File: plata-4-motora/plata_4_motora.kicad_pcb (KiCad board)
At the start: 2 copper layers, 141 x 90 mm, 28 parts, among them M0 мотор 0, M1 мотор 1, M2 мотор 2, M3 мотор 3, U0B S2209, U0T S2209, U1B S2209, U1T S2209, U2B S2209, U2T S2209, U3B S2209, U3T S2209

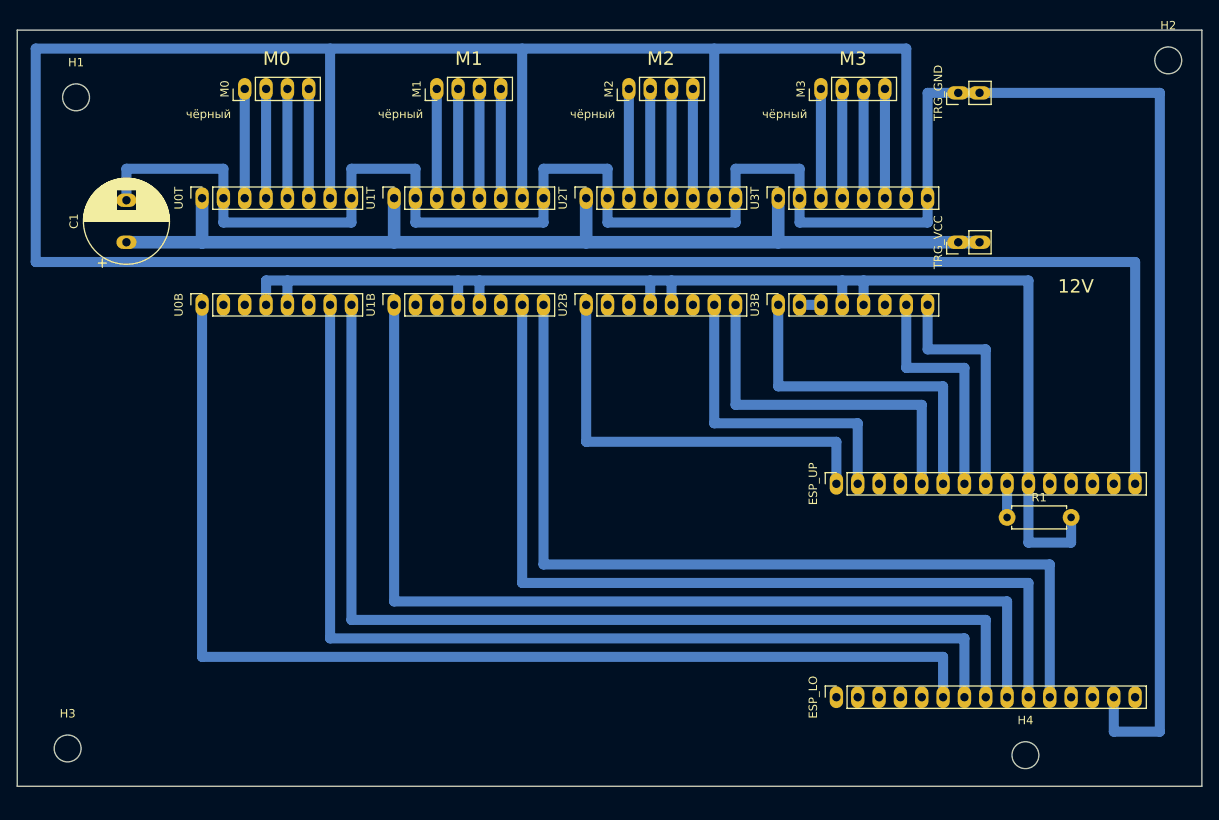
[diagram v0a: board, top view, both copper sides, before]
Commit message: Плата 4 моторов: компактная 92x92 (рисунок 65x89) под заготовку 100x100 — драйверы 2+2, ESP посередине; G-code за одну установку; вики 9.7–9.9
Co-Authored-By: Claude Fable 5.1 <noreply@anthropic.com>
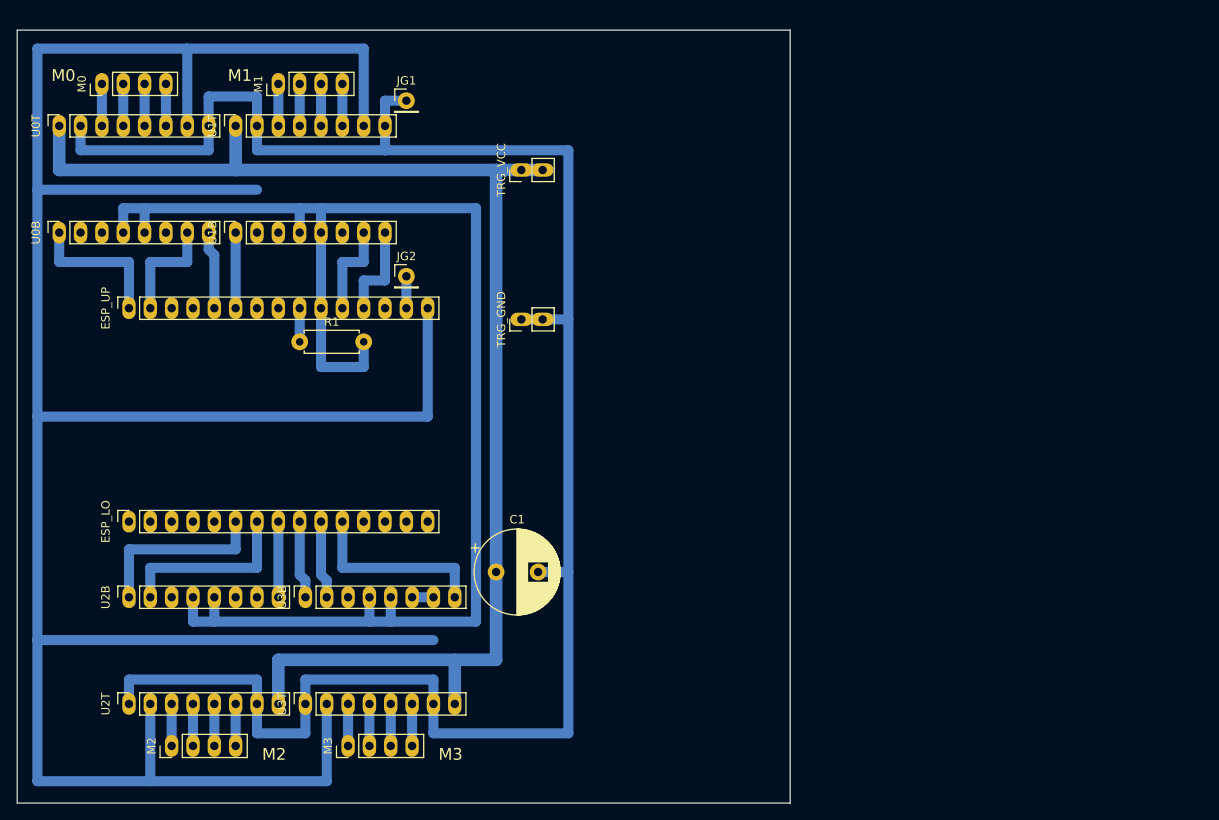
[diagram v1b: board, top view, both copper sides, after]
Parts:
- removed H1, H2, H3, H4: MountingHole_3.2mm_M3, MountingHole_3.2mm_M3
- added JG1: PinHeader_1x01_P2.54mm_Vertical, PinHeader_1x01_P2.54mm_Vertical, F.Cu at (46.3, 8.40)
- added JG2: PinHeader_1x01_P2.54mm_Vertical, PinHeader_1x01_P2.54mm_Vertical, F.Cu at (46.3, 29.3)
- moved M3 96.3 mm to (39.4, 85.2)
- moved M2 95.3 mm to (18.4, 85.2)
- moved ESP 86.8 mm to (31.6, 45.8)
- moved ESP_LO 86.8 mm to (13.3, 58.5)
- moved ESP_UP 86.8 mm to (13.3, 33.1)
- moved R1 86.8 mm to (33.6, 37.1)
- moved U3T 82.4 mm to (34.3, 80.2)
- moved U2T 81.2 mm to (13.3, 80.2)
- moved DRV3 73.6 mm to (43.2, 73.8)
- moved DRV2 72.2 mm to (22.2, 73.8)
- moved U3B 66.2 mm to (34.3, 67.5)
- moved U2B 64.6 mm to (13.3, 67.5)
- moved C1 59.0 mm to (57.0, 64.5), turned to 0 degrees
- moved TRG_GND 58.6 mm to (60.0, 34.4)
- moved TRG 52.8 mm to (73.7, 25.5)
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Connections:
- ESP_LO pad 10: STEP1 -> STEP3
- ESP_LO pad 11: DIR1 -> EN3
- ESP_LO pad 14: GND -> (no net)
- ESP_LO pad 6: EN0 -> DIR2
- ESP_LO pad 7: STEP0 -> STEP2
- ESP_LO pad 8: DIR0 -> EN2
- ESP_LO pad 9: EN1 -> DIR3
- ESP_UP pad 1: EN2 -> EN0
- ESP_UP pad 11: (no net) -> STEP1
- ESP_UP pad 12: (no net) -> DIR1
- ESP_UP pad 14: (no net) -> GND
- ESP_UP pad 2: STEP2 -> STEP0
- ESP_UP pad 5: DIR2 -> DIR0
- ESP_UP pad 6: EN3 -> EN1
- ESP_UP pad 7: STEP3 -> (no net)
- ESP_UP pad 8: DIR3 -> (no net)
- M2 pad 1: M2_A2 -> M2_B2
- M2 pad 2: M2_A1 -> M2_B1
- M2 pad 3: M2_B1 -> M2_A1
- M2 pad 4: M2_B2 -> M2_A2
- M3 pad 1: M3_A2 -> M3_B2
- M3 pad 2: M3_A1 -> M3_B1
- M3 pad 3: M3_B1 -> M3_A1
- M3 pad 4: M3_B2 -> M3_A2
- U2B pad 1: EN2 -> DIR2
- U2B pad 2: (no net) -> STEP2
- U2B pad 3: VIO -> (no net)
- U2B pad 6: (no net) -> VIO
- U2B pad 7: STEP2 -> (no net)
- U2B pad 8: DIR2 -> EN2
- U2T pad 1: VM -> GND
- U2T pad 2: GND -> VIO
- U2T pad 3: M2_A2 -> M2_B2
- U2T pad 4: M2_A1 -> M2_B1
- U2T pad 5: M2_B1 -> M2_A1
- U2T pad 6: M2_B2 -> M2_A2
- U2T pad 7: VIO -> GND
- U2T pad 8: GND -> VM
- U3B pad 1: EN3 -> DIR3
- U3B pad 2: VIO -> STEP3
- U3B pad 3: VIO -> (no net)
- U3B pad 6: (no net) -> VIO
- U3B pad 7: STEP3 -> VIO
- U3B pad 8: DIR3 -> EN3
- U3T pad 1: VM -> GND
- U3T pad 2: GND -> VIO
- U3T pad 3: M3_A2 -> M3_B2
- U3T pad 4: M3_A1 -> M3_B1
- U3T pad 5: M3_B1 -> M3_A1
- U3T pad 6: M3_B2 -> M3_A2
- U3T pad 7: VIO -> GND
- U3T pad 8: GND -> VM
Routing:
- net EN0: track 134.9 -> 17.3 mm
- net DIR0: track 122.2 -> 9.28 mm
- net EN1: track 119.7 -> 9.00 mm
- net STEP0: track 122.2 -> 13.4 mm
- net DIR1: track 107.0 -> 11.5 mm
- net STEP1: track 107.0 -> 11.5 mm
- net EN2: track 51.1 -> 9.00 mm
- net VM: track 122.5 -> 162.8 mm
- net GND: track 272.6 -> 239.0 mm
- net VIO: track 360.0 -> 332.5 mm
- net DIR2: track 43.5 -> 21.7 mm
- net STEP3: track 28.2 -> 9.28 mm
- net DIR3: track 28.2 -> 9.28 mm
- net UART: track 153.2 -> 172.1 mm
- net EN3: track 40.9 -> 22.4 mm
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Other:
- board size 141 x 90 mm -> 92 x 92 mm
- board text removed: "12V"
- board text removed: "чёрный"
